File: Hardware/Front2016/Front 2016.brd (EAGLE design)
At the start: 100 x 100 mm, 177 parts

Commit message: Connecting the seconds
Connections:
- new net N$13: ICH13.1, SEC17.C
- new net N$14: ICH9.1, SEC11.C
- new net N$15: ICH9.2, SEC12.C
- new net N$16: ICH9.3, SEC13.C
- new net N$17: ICH26.2, SEC38.C
- new net N$18: ICH10.1, SEC14.C
- new net N$19: ICH10.2, SEC15.C
- new net N$20: ICH10.3, SEC16.C
- new net N$21: ICH14.1, SEC20.C
- new net N$22: ICH13.2, SEC18.C
- new net N$23: ICH13.3, SEC19.C
- new net N$24: ICH14.2, SEC21.C
- new net N$25: ICH14.3, SEC22.C
- new net N$26: ICH26.3, SEC40.C
- new net N$27: ICH17.1, SEC23.C
- new net N$28: ICH17.2, SEC24.C
- new net N$29: ICH17.3, SEC25.C
- new net N$30: ICH18.1, SEC26.C
- new net N$31: ICH18.2, SEC27.C
- new net N$32: ICH18.3, SEC28.C
- new net N$33: ICH30.6
- new net N$34: ICH29.1, SEC41.C
- new net N$35: ICH21.1, SEC29.C
- new net N$36: ICH21.2, SEC31.C
- new net N$37: ICH21.3, SEC30.C
- new net N$38: ICH29.2, SEC42.C
- new net N$39: ICH22.1, SEC32.C
- new net N$40: ICH22.2, SEC33.C
- new net N$41: ICH22.3, SEC34.C
- new net N$42: ICH29.3, SEC43.C
- new net N$43: ICH25.1, SEC35.C
- new net N$44: ICH25.2, SEC36.C
- new net N$45: ICH25.3, SEC37.C
- new net N$46: ICH30.5, ICH33.6
- new net N$47: ICH26.1, SEC39.C
- new net N$48: ICH30.1, SEC44.C
- new net N$49: ICH30.2, SEC45.C
- new net N$50: ICH30.3, SEC46.C
- new net N$51: ICH33.5, ICH34.6
- new net N$52: ICH33.1, SEC47.C
- new net N$53: ICH33.2, SEC48.C
- new net N$54: ICH33.3, SEC49.C
- new net N$55: ICH34.5, ICH37.6
- new net N$56: ICH34.1, SEC50.C
- new net N$57: ICH34.2, SEC51.C
- new net N$58: ICH34.3, SEC52.C
- new net N$59: ICH37.5, ICH41.6
- new net N$60: ICH37.1, SEC53.C
- new net N$61: ICH37.2, SEC54.C
- new net N$62: ICH37.3, SEC55.C
- new net N$64: ICH41.1, SEC56.C
- new net N$65: ICH41.2, SEC57.C
- new net N$66: ICH41.3, SEC58.C
- new net N$67: ICH1.5, ICH2.6
- new net N$68: ICH2.5, ICH5.6
- new net N$69: ICH5.5, ICH6.6
- new net N$70: ICH6.5, ICH9.6
- new net N$71: ICH10.6, ICH9.5
- new net N$72: ICH10.5, ICH13.6
- new net N$73: ICH13.5, ICH14.6
- new net N$74: ICH14.5, ICH17.6
- new net N$75: ICH17.5, ICH18.6
- new net N$76: ICH18.5, ICH21.6
- new net N$77: ICH21.5, ICH22.6
- new net N$78: ICH22.5, ICH25.6
- new net N$79: ICH25.5, ICH26.6
- new net N$80: ICH26.5, ICH29.6
- net 5V: now also SEC11.A, SEC12.A, SEC13.A, SEC14.A, SEC15.A, SEC16.A, SEC17.A, SEC18.A, SEC19.A, SEC20.A, SEC21.A, SEC22.A, SEC23.A, SEC24.A, SEC25.A, SEC26.A, SEC27.A, SEC28.A, SEC29.A, SEC30.A, SEC31.A, SEC32.A, SEC33.A, SEC34.A, SEC35.A, SEC36.A, SEC37.A, SEC38.A, SEC39.A, SEC40.A, SEC41.A, SEC42.A, SEC43.A, SEC44.A, SEC45.A, SEC46.A, SEC47.A, SEC48.A, SEC49.A, SEC50.A, SEC51.A, SEC52.A, SEC53.A, SEC54.A, SEC55.A, SEC56.A, SEC57.A, SEC58.A

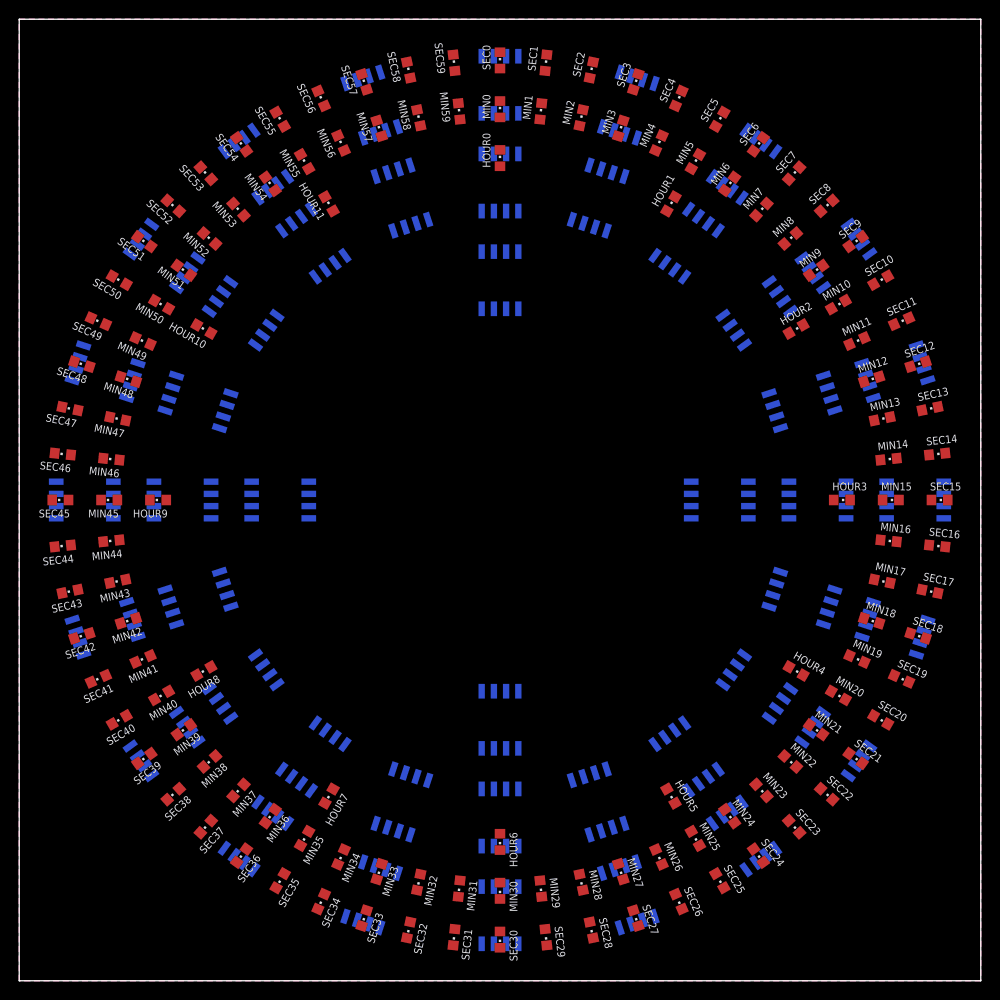
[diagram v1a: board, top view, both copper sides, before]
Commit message: Connected rest of schematic, added solderpad for +5V, DIN, DOUT, GND Added a footprint for a capacitor in the ws8211 footprint
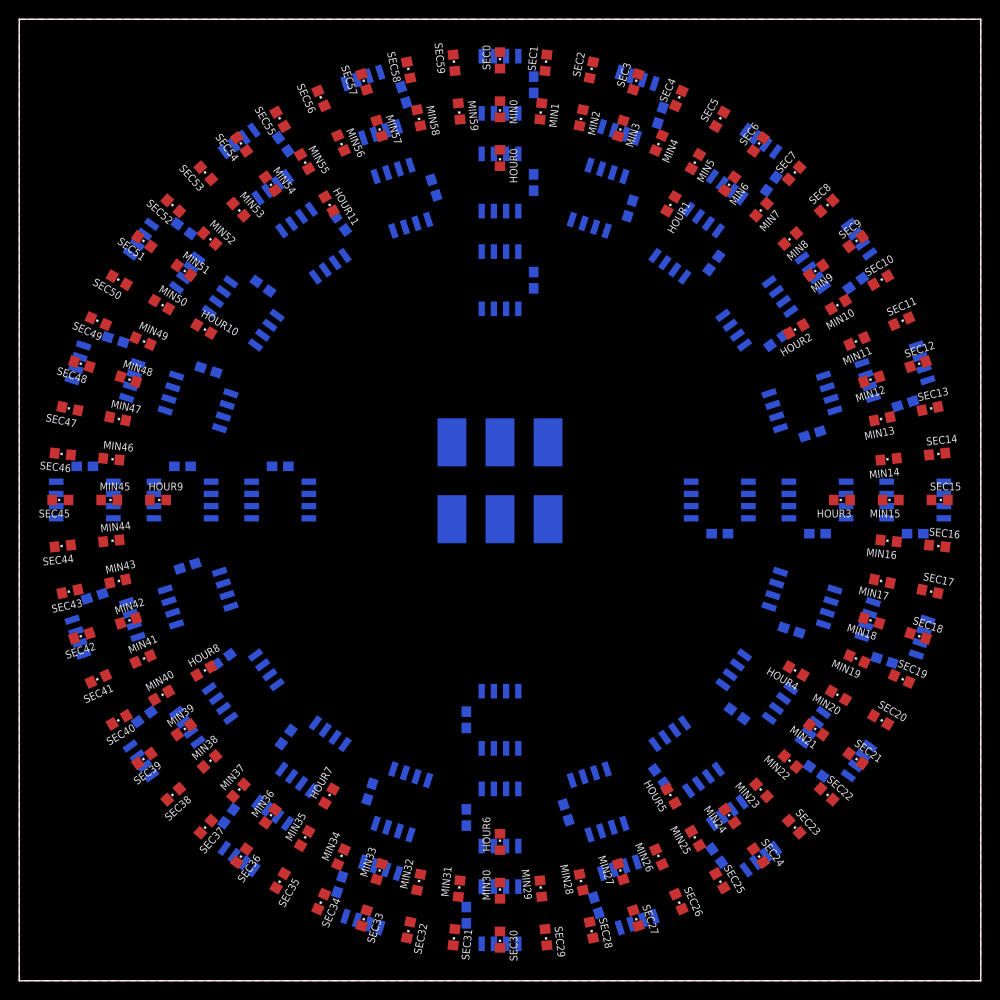
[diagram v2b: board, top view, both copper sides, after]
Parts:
- added +5V, +5V1, DIN, DOUT, GND, GND46: SOLDER_PAD, timearc:SOLDER_PAD
- ICC1, ICC2, ICC3, ICC4, ICH1, ICH10, ICH13, ICH14, ICH17, ICH18, ICH2, ICH21, ICH22, ICH25, ICH26, ICH29, ICH30, ICH33, ICH34, ICH37, ICH41, ICH5, ICH6, ICH9, ICL11, ICL12, ICL15, ICL16, ICL19, ICL20, ICL23, ICL24, ICL27, ICL28, ICL3, ICL31, ICL32, ICL35, ICL36, ICL39, ICL4, ICL43, ICL7, ICL8: device adafruit:SO08-SKINNYPADS -> timearc:SO08-SKINNYPADS
- turned HOUR0 to 180 degrees
- turned HOUR1 to 150 degrees
- turned HOUR10 to 240 degrees
- turned HOUR11 to 210 degrees
- turned HOUR2 to 120 degrees
- turned HOUR3 to 90 degrees
- turned HOUR4 to 60 degrees
- turned HOUR5 to 30 degrees
- turned HOUR6 to 0 degrees
- turned HOUR7 to 330 degrees
- turned HOUR8 to 300 degrees
- turned HOUR9 to 270 degrees
- turned ICC1 to 180 degrees
- turned ICC2 to 270 degrees
- turned ICC3 to 0 degrees
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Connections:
- new net N$100: ICL12.2, MIN15.C
- new net N$101: ICL12.3, MIN16.C
- new net N$102: ICL11.6, ICL8.5
- new net N$103: ICL15.1, MIN17.C
- new net N$104: ICL15.2, MIN18.C
- new net N$105: ICL15.3, MIN19.C
- new net N$106: ICL11.5, ICL12.6
- new net N$107: ICL16.1, MIN20.C
- new net N$108: ICL16.2, MIN21.C
- new net N$109: ICL16.3, MIN22.C
- new net N$110: ICL12.5, ICL15.6
- new net N$111: ICL19.1, MIN23.C
- new net N$112: ICL19.2, MIN24.C
- new net N$113: ICL19.3, MIN25.C
- new net N$114: ICL15.5, ICL16.6
- new net N$115: ICL20.1, MIN26.C
- new net N$116: ICL20.2, MIN27.C
- new net N$117: ICL20.3, MIN28.C
- new net N$118: ICL16.5, ICL19.6
- new net N$119: ICL23.1, MIN29.C
- new net N$120: ICL23.2, MIN30.C
- new net N$121: ICL23.3, MIN31.C
- new net N$122: ICL19.5, ICL20.6
- new net N$123: ICL24.1, MIN32.C
- new net N$124: ICL24.2, MIN33.C
- new net N$125: ICL24.3, MIN34.C
- new net N$126: ICL20.5, ICL23.6
- new net N$127: ICL27.1, MIN35.C
- new net N$128: ICL27.2, MIN36.C
- new net N$129: ICL27.3, MIN37.C
- new net N$130: ICL23.5, ICL24.6
- new net N$131: ICL28.1, MIN38.C
- new net N$132: ICL28.2, MIN39.C
- new net N$133: ICL28.3, MIN40.C
- new net N$134: ICL24.5, ICL27.6
- new net N$135: ICL31.1, MIN41.C
- new net N$136: ICL31.2, MIN42.C
- new net N$137: ICL31.3, MIN43.C
- new net N$138: ICL27.5, ICL28.6
- new net N$139: ICL32.1, MIN44.C
- new net N$140: ICL32.2, MIN45.C
- new net N$141: ICL32.3, MIN46.C
- new net N$142: ICL28.5, ICL31.6
- new net N$143: ICL35.1, MIN47.C
- new net N$144: ICL35.2, MIN48.C
- new net N$145: ICL35.3, MIN49.C
- new net N$146: ICL31.5, ICL32.6
- new net N$147: ICL36.1, MIN50.C
- new net N$148: ICL36.2, MIN51.C
- new net N$149: ICL36.3, MIN52.C
- new net N$150: ICL32.5, ICL35.6
- new net N$151: ICL39.1, MIN53.C
- new net N$152: ICL39.2, MIN54.C
- new net N$153: ICL39.3, MIN55.C
- new net N$154: ICL35.5, ICL36.6
- new net N$155: ICL43.1, MIN56.C
- new net N$156: ICL43.2, MIN57.C
- new net N$157: ICL43.3, MIN58.C
- new net N$158: ICL36.5, ICL39.6
- new net N$159: ICL39.5, ICL43.6
- new net N$160: DIN.1, ICH1.6
- new net N$161: HOUR11.C, ICC1.1
- new net N$162: HOUR0.C, ICC1.2
- new net N$163: HOUR1.C, ICC1.3
- new net N$164: DOUT.1, ICC4.5
- new net N$165: HOUR2.C, ICC2.1
- new net N$166: HOUR3.C, ICC2.2
- new net N$167: HOUR4.C, ICC2.3
- new net N$169: HOUR5.C, ICC3.1
- new net N$170: HOUR6.C, ICC3.2
- new net N$171: HOUR7.C, ICC3.3
- new net N$173: HOUR8.C, ICC4.1
- new net N$174: HOUR9.C, ICC4.2
- new net N$175: HOUR10.C, ICC4.3
- new net N$176: ICC1.6, ICL43.5
- new net N$177: ICC1.5, ICC2.6
- new net N$178: ICC2.5, ICC3.6
- new net N$179: ICC3.5, ICC4.6
- new net N$63: ICH41.5, ICL3.6
- new net N$81: ICL3.1, MIN59.C
- new net N$82: ICL3.2, MIN0.C
- new net N$83: ICL3.3, MIN1.C
- new net N$84: ICL4.1, MIN2.C
- new net N$85: ICL4.2, MIN3.C
- new net N$86: ICL4.3, MIN4.C
- new net N$87: ICL7.1, MIN5.C
- new net N$88: ICL7.2, MIN6.C
- new net N$89: ICL7.3, MIN7.C
- new net N$90: ICL8.1, MIN8.C
- new net N$91: ICL8.2, MIN9.C
- new net N$92: ICL8.3, MIN10.C
- new net N$93: ICL3.5, ICL4.6
- new net N$94: ICL4.5, ICL7.6
- new net N$95: ICL11.1, MIN11.C
- new net N$96: ICL11.2, MIN12.C
- new net N$97: ICL11.3, MIN13.C
- new net N$98: ICL7.5, ICL8.6
- new net N$99: ICL12.1, MIN14.C
- net 5V: now also +5V.1, +5V1.1, HOUR0.A, HOUR1.A, HOUR10.A, HOUR11.A, HOUR2.A, HOUR3.A, HOUR4.A, HOUR5.A, HOUR6.A, HOUR7.A, HOUR8.A, HOUR9.A, ICC1.+5V, ICC2.+5V, ICC3.+5V, ICC4.+5V, ICH1.+5V, ICH10.+5V, ICH13.+5V, ICH14.+5V, ICH17.+5V, ICH18.+5V, ICH2.+5V, ICH21.+5V, ICH22.+5V, ICH25.+5V, ICH26.+5V, ICH29.+5V, ICH30.+5V, ICH33.+5V, ICH34.+5V, ICH37.+5V, ICH41.+5V, ICH5.+5V, ICH6.+5V, ICH9.+5V, ICL11.+5V, ICL12.+5V, ICL15.+5V, ICL16.+5V, ICL19.+5V, ICL20.+5V, ICL23.+5V, ICL24.+5V, ICL27.+5V, ICL28.+5V, ICL3.+5V, ICL31.+5V, ICL32.+5V, ICL35.+5V, ICL36.+5V, ICL39.+5V, ICL4.+5V, ICL43.+5V, ICL7.+5V, ICL8.+5V, MIN0.A, MIN1.A, MIN10.A, MIN11.A, MIN12.A, MIN13.A, MIN14.A, MIN15.A, MIN16.A, MIN17.A, MIN18.A, MIN19.A, MIN2.A, MIN20.A, MIN21.A, MIN22.A, MIN23.A, MIN24.A, MIN25.A, MIN26.A, MIN27.A, MIN28.A, MIN29.A, MIN3.A, MIN30.A, MIN31.A, MIN32.A, MIN33.A, MIN34.A, MIN35.A, MIN36.A, MIN37.A, MIN38.A, MIN39.A, MIN4.A, MIN40.A, MIN41.A, MIN42.A, MIN43.A, MIN44.A, MIN45.A, MIN46.A, MIN47.A, MIN48.A, MIN49.A, MIN5.A, MIN50.A, MIN51.A, MIN52.A, MIN53.A, MIN54.A, MIN55.A, MIN56.A, MIN57.A, MIN58.A, MIN59.A, MIN6.A, MIN7.A, MIN8.A, MIN9.A
- net GND: now also GND.1, GND46.1, ICC1.GND, ICC2.GND, ICC3.GND, ICC4.GND, ICH1.GND, ICH10.GND, ICH13.GND, ICH14.GND, ICH17.GND, ICH18.GND, ICH2.GND, ICH21.GND, ICH22.GND, ICH25.GND, ICH26.GND, ICH29.GND, ICH30.GND, ICH33.GND, ICH34.GND, ICH37.GND, ICH41.GND, ICH5.GND, ICH6.GND, ICH9.GND, ICL11.GND, ICL12.GND, ICL15.GND, ICL16.GND, ICL19.GND, ICL20.GND, ICL23.GND, ICL24.GND, ICL27.GND, ICL28.GND, ICL3.GND, ICL31.GND, ICL32.GND, ICL35.GND, ICL36.GND, ICL39.GND, ICL4.GND, ICL43.GND, ICL7.GND, ICL8.GND
- net N$33: now also ICH29.5

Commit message: 100% routed, Updated the TIMEARC_KEEPOUT footprint to include the 4 drill holes
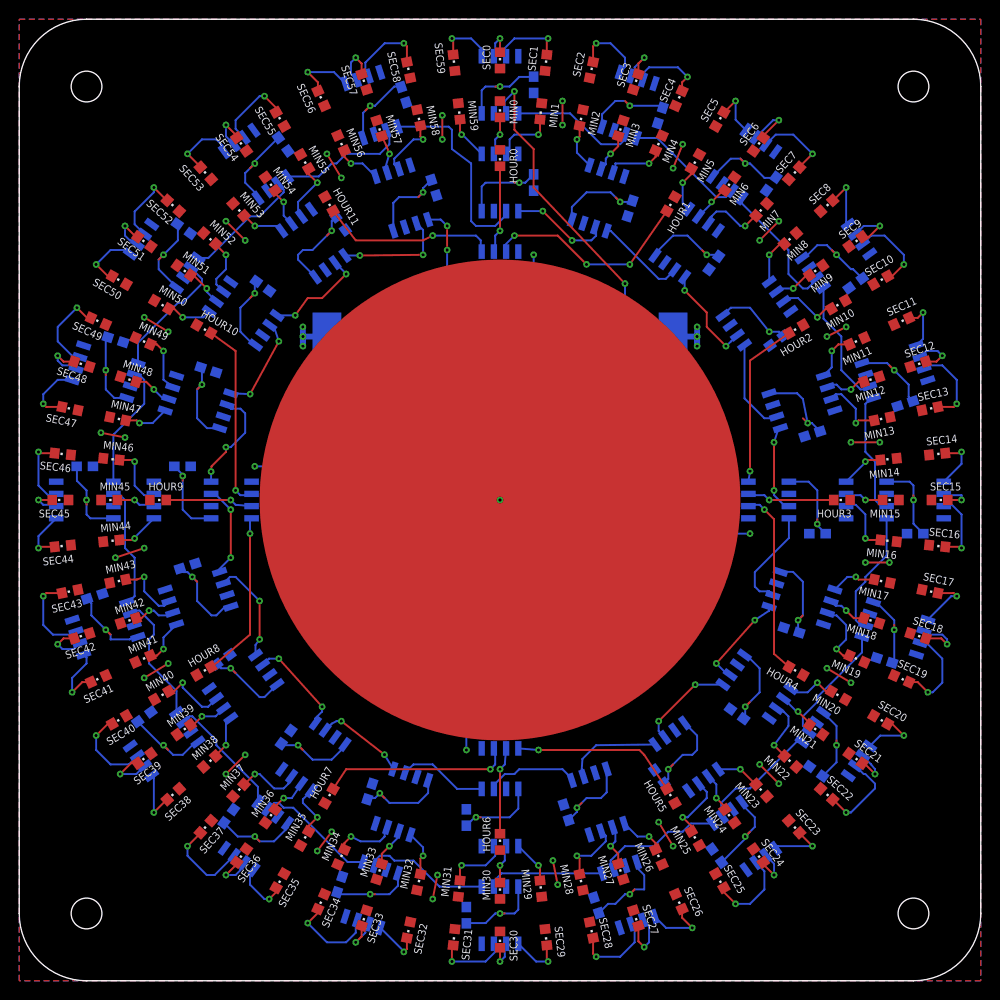
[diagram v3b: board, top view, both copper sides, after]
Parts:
- added GND48, TOUCH: SOLDER_PAD, timearc:SOLDER_PAD
- added U$2: TOUCH_PAD_LARGE, timearc:TOUCH_PAD_LARGE
- moved +5V 25.5 mm to (68.0, 67.0)
- moved +5V1 23.0 mm to (32.0, 67.0)
- moved DOUT 23.0 mm to (37.0, 67.0)
- moved GND46 23.0 mm to (42.0, 67.0)
- moved DIN 17.0 mm to (63.0, 67.0)
- moved GND 11.4 mm to (58.0, 67.0)
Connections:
- new net TOUCH: TOUCH.1, U$2.P$1, U$2.P$2
- net GND: now also GND48.1
- net N$17: now also SEC39.C; no longer SEC38.C
- net N$36: now also SEC30.C; no longer SEC31.C
- net N$37: now also SEC31.C; no longer SEC30.C
- net N$47: now also SEC38.C; no longer SEC39.C
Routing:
- net 5V: track 0.00 -> 409.7 mm, vias 0 -> 50
- net GND: track 0.00 -> 54.6 mm, vias 0 -> 40
- net N$160: track 0.00 -> 32.9 mm, vias 0 -> 2
- net N$178: track 0.00 -> 29.3 mm
- net N$179: track 0.00 -> 29.0 mm
- net N$177: track 0.00 -> 29.0 mm
- net N$163: track 0.00 -> 22.1 mm, vias 0 -> 3
- net N$63: track 0.00 -> 21.0 mm
- net N$171: track 0.00 -> 19.9 mm, vias 0 -> 1
- net N$175: track 0.00 -> 19.6 mm, vias 0 -> 1
- net N$167: track 0.00 -> 19.4 mm, vias 0 -> 1
- net N$176: track 0.00 -> 18.6 mm, vias 0 -> 2
- net N$161: track 0.00 -> 18.4 mm, vias 0 -> 1
- net N$164: track 0.00 -> 17.9 mm
- net N$169: track 0.00 -> 17.6 mm, vias 0 -> 1
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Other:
- outline, holes or cut-outs redrawn

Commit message: Logo and silkscreen
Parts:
- added U$3: (no value), timearc:TIMEARC_LOGO_SIMPLE
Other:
- board text added: "I"
- board text added: "II"
- board text added: "III"
- board text added: "IV"
- board text added: "IX"
- board text added: "Time Arc, Front Armin Oonk, APR2016"
- board text added: "V"
- board text added: "VI"
- board text added: "VII"
- board text added: "VIII"
- board text added: "X"
- board text added: "XI"
- board text added: "XII"
